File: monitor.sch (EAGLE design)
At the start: 60 parts, among them IC1 LM1117-5, IC2 LM1117-5, J3 DCJ0202, J4 DCJ0202, J5 DCJ0202, Q1 IRLML2502, T1 BC846, X3 PN61729-S, X4 PN87520-S

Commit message: SPI to PGA
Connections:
- new net OE: U$1G$2.PE6, U$4G$9.OE
- net /CS: now also U$4G$3.IOVCC; no longer U$4G$1.IOVCC
- net CLK: now also U$4G$7.IOVCC; no longer U$4G$2.IOVCC
- net DIN: now also U$4G$5.IOVCC; no longer U$4G$4.IOVCC
- net DOUT: now also U$4G$1.IOVCC; no longer U$4G$3.IOVCC
- net I2C3_SCL: now also U$4G$8.IOVL; no longer U$4G$6.IOVL
- net I2C3_SDA: now also U$4G$6.IOVL; no longer U$4G$5.IOVL
- net SCL: now also U$4G$8.IOVCC; no longer U$4G$6.IOVCC
- net SDA: now also U$4G$6.IOVCC; no longer U$4G$5.IOVCC
- net SPI2_MISO: now also U$4G$1.IOVL; no longer U$4G$3.IOVL
- net SPI2_MOSI: now also U$4G$5.IOVL; no longer U$4G$4.IOVL
- net SPI2_NSS: now also U$4G$3.IOVL; no longer U$4G$1.IOVL
- net SPI2_SCK: now also U$4G$7.IOVL; no longer U$4G$2.IOVL
- net VDD: no longer U$1G$2.VDD
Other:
- moved on the sheet: U$4G$1, U$4G$2, U$4G$3, U$4G$4, U$4G$5, U$4G$6
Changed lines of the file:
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@@
 <part name="VDD1" library="supply1" deviceset="VDD" device=""/>
 <part name="VDD2" library="supply1" deviceset="VDD" device=""/>
-<part name="VDD3" library="supply1" deviceset="VDD" device=""/>
 <part name="P+1" library="supply1" deviceset="+5V" device=""/>
 <part name="VDD4" library="supply1" deviceset="VDD" device=""/>
@@
 <instance part="U$3" gate="G$1" x="139.7" y="60.96"/>
 <instance part="GND16" gate="1" x="144.78" y="38.1"/>
-<instance part="U$4" gate="G$1" x="73.66" y="109.22"/>
-<instance part="U$4" gate="G$2" x="73.66" y="99.06"/>
-<instance part="U$4" gate="G$3" x="73.66" y="88.9"/>
-<instance part="U$4" gate="G$4" x="73.66" y="78.74"/>
-<instance part="U$4" gate="G$5" x="73.66" y="68.58"/>
-<instance part="U$4" gate="G$6" x="73.66" y="58.42"/>
+<instance part="U$4" gate="G$3" x="73.66" y="109.22"/>
+<instance part="U$4" gate="G$7" x="73.66" y="99.06"/>
+<instance part="U$4" gate="G$1" x="73.66" y="88.9"/>
+<instance part="U$4" gate="G$5" x="73.66" y="78.74"/>
+<instance part="U$4" gate="G$6" x="73.66" y="68.58"/>
+<instance part="U$4" gate="G$8" x="73.66" y="58.42"/>
 <instance part="U$4" gate="G$9" x="30.48" y="68.58"/>
 <instance part="GND15" gate="1" x="231.14" y="66.04"/>
@@
 <instance part="F1" gate="G$1" x="78.74" y="144.78"/>
 <instance part="D3" gate="1" x="91.44" y="137.16" rot="R90"/>
+<instance part="U$4" gate="G$2" x="73.66" y="48.26"/>
+<instance part="U$4" gate="G$4" x="73.66" y="38.1"/>
 </instances>
 <busses>
@@
 <wire x1="58.42" y1="109.22" x2="48.26" y2="109.22" width="0.1524" layer="91"/>
 <label x="48.26" y="109.22" size="1.778" layer="95"/>
-<pinref part="U$4" gate="G$1" pin="IOVL"/>
+<pinref part="U$4" gate="G$3" pin="IOVL"/>
 </segment>
 </net>
@@
 <wire x1="58.42" y1="88.9" x2="48.26" y2="88.9" width="0.1524" layer="91"/>
 <label x="48.26" y="88.9" size="1.778" layer="95"/>
-<pinref part="U$4" gate="G$3" pin="IOVL"/>
+<pinref part="U$4" gate="G$1" pin="IOVL"/>
 </segment>
 </net>
@@
 <wire x1="58.42" y1="99.06" x2="48.26" y2="99.06" width="0.1524" layer="91"/>
 <label x="48.26" y="99.06" size="1.778" layer="95"/>
-<pinref part="U$4" gate="G$2" pin="IOVL"/>
+<pinref part="U$4" gate="G$7" pin="IOVL"/>
 </segment>
 </net>
@@
 <wire x1="58.42" y1="78.74" x2="48.26" y2="78.74" width="0.1524" layer="91"/>
 <label x="48.26" y="78.74" size="1.778" layer="95"/>
-<pinref part="U$4" gate="G$4" pin="IOVL"/>
+<pinref part="U$4" gate="G$5" pin="IOVL"/>
 </segment>
 </net>
@@
 <wire x1="91.44" y1="109.22" x2="99.06" y2="109.22" width="0.1524" layer="91"/>
 <label x="93.98" y="109.22" size="1.778" layer="95"/>
-<pinref part="U$4" gate="G$1" pin="IOVCC"/>
+<pinref part="U$4" gate="G$3" pin="IOVCC"/>
 </segment>
 <segment>
@@
 <wire x1="91.44" y1="99.06" x2="99.06" y2="99.06" width="0.1524" layer="91"/>
 <label x="93.98" y="99.06" size="1.778" layer="95"/>
-<pinref part="U$4" gate="G$2" pin="IOVCC"/>
+<pinref part="U$4" gate="G$7" pin="IOVCC"/>
 </segment>
 <segment>
@@
 <wire x1="91.44" y1="88.9" x2="99.06" y2="88.9" width="0.1524" layer="91"/>
 <label x="93.98" y="88.9" size="1.778" layer="95"/>
-<pinref part="U$4" gate="G$3" pin="IOVCC"/>
+<pinref part="U$4" gate="G$1" pin="IOVCC"/>
 </segment>
 <segment>
@@
 <wire x1="91.44" y1="78.74" x2="99.06" y2="78.74" width="0.1524" layer="91"/>
 <label x="93.98" y="78.74" size="1.778" layer="95"/>
-<pinref part="U$4" gate="G$4" pin="IOVCC"/>
+<pinref part="U$4" gate="G$5" pin="IOVCC"/>
 </segment>
 <segment>
@@
 <net name="I2C3_SCL" class="0">
 <segment>
-<pinref part="U$4" gate="G$6" pin="IOVL"/>
+<pinref part="U$4" gate="G$8" pin="IOVL"/>
 <wire x1="48.26" y1="58.42" x2="58.42" y2="58.42" width="0.1524" layer="91"/>
 <label x="48.26" y="58.42" size="1.778" layer="95"/>
@@
 </segment>
 <segment>
-<pinref part="U$4" gate="G$5" pin="IOVCC"/>
+<pinref part="U$4" gate="G$6" pin="IOVCC"/>
 <wire x1="91.44" y1="68.58" x2="99.06" y2="68.58" width="0.1524" layer="91"/>
 <label x="93.98" y="68.58" size="1.778" layer="95"/>
@@
 </segment>
 <segment>
-<pinref part="U$4" gate="G$6" pin="IOVCC"/>
+<pinref part="U$4" gate="G$8" pin="IOVCC"/>
 <wire x1="91.44" y1="58.42" x2="99.06" y2="58.42" width="0.1524" layer="91"/>
 <label x="93.98" y="58.42" size="1.778" layer="95"/>
@@
 <net name="I2C3_SDA" class="0">
 <segment>
-<pinref part="U$4" gate="G$5" pin="IOVL"/>
+<pinref part="U$4" gate="G$6" pin="IOVL"/>
 <wire x1="58.42" y1="68.58" x2="48.26" y2="68.58" width="0.1524" layer="91"/>
 <label x="48.26" y="68.58" size="1.778" layer="95"/>
@@
 <pinref part="JP1" gate="B" pin="1"/>
 <wire x1="106.68" y1="147.32" x2="139.7" y2="147.32" width="0.1524" layer="91"/>
+</segment>
+</net>
+<net name="OE" class="0">
+<segment>
+<pinref part="U$4" gate="G$9" pin="OE"/>
+<wire x1="17.78" y1="68.58" x2="10.16" y2="68.58" width="0.1524" layer="91"/>
+<label x="10.16" y="68.58" size="1.778" layer="95"/>
 </segment>
 </net>
@@
 <instance part="VDD1" gate="G$1" x="91.44" y="109.22" rot="R270"/>
 <instance part="VDD2" gate="G$1" x="22.86" y="109.22" rot="R90"/>
-<instance part="VDD3" gate="G$1" x="236.22" y="86.36" rot="R270"/>
 <instance part="P+4" gate="1" x="167.64" y="109.22" smashed="yes" rot="R90">
 <attribute name="VALUE" x="167.64" y="109.22" size="1.778" layer="96" rot="R180"/>
@@
 <pinref part="VDD2" gate="G$1" pin="VDD"/>
 </segment>
-<segment>
-<pinref part="U$1" gate="G$2" pin="VDD"/>
-<pinref part="VDD3" gate="G$1" pin="VDD"/>
-</segment>
 </net>
 <net name="+5V" class="0">
@@
 </segment>
 </net>
+<net name="OE" class="0">
+<segment>
+<pinref part="U$1" gate="G$2" pin="PE6"/>
+<wire x1="170.18" y1="99.06" x2="162.56" y2="99.06" width="0.1524" layer="91"/>
+<label x="162.56" y="99.06" size="1.778" layer="95"/>
+</segment>
+</net>

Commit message: All chips connected
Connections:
- net OUT: no longer U$2.V6
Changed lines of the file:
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@@
 <instance part="F1" gate="G$1" x="78.74" y="144.78"/>
 <instance part="D3" gate="1" x="91.44" y="137.16" rot="R90"/>
-<instance part="U$4" gate="G$2" x="73.66" y="48.26"/>
-<instance part="U$4" gate="G$4" x="73.66" y="38.1"/>
 </instances>
 <busses>
@@
 <junction x="154.94" y="142.24"/>
 </segment>
-<segment>
-<pinref part="U$2" gate="G$1" pin="V6"/>
-<wire x1="187.96" y1="68.58" x2="177.8" y2="68.58" width="0.1524" layer="91"/>
-<label x="177.8" y="68.58" size="1.4224" layer="95"/>
-</segment>
-</net>
+</net>

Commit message: All connected (not routed), updated STM32F4Discovery layout
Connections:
- net B_DOWN: now also U$1G$2.PB7
- net B_ESC: now also U$1G$2.PB5
- net B_LEFT: now also U$1G$2.PE5
- net B_OK: now also U$1G$2.PE3
- net B_RIGHT: now also U$1G$2.PB8
- net B_UP: now also U$1G$2.PE4
- net LCD_CS1: now also U$1G$1.PA2; no longer U$1G$1.PA2/ETH_MDIO
- net LCD_CS2: now also U$1G$1.PC4; no longer U$1G$1.PC4/ETH_MII_RX_D0
- net SPI2_NSS: now also U$1G$1.PB12; no longer U$1G$1.PB12/ETH_MII_TXD0
- net SPI2_SCK: now also U$1G$1.PB13; no longer U$1G$1.PB13/ETH_MII_TXD1
- net VDD: now also U$1G$1.VDD1, U$1G$1.VDD2; no longer U$1G$1.VDO1, U$1G$1.VDO2
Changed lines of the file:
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@@
 <net name="SPI2_NSS" class="0">
 <segment>
-<pinref part="U$1" gate="G$1" pin="PB12/ETH_MII_TXD0"/>
+<pinref part="U$1" gate="G$1" pin="PB12"/>
 <wire x1="88.9" y1="68.58" x2="96.52" y2="68.58" width="0.1524" layer="91"/>
 <label x="96.52" y="68.58" size="1.778" layer="95"/>
@@
 <net name="SPI2_SCK" class="0">
 <segment>
-<pinref part="U$1" gate="G$1" pin="PB13/ETH_MII_TXD1"/>
+<pinref part="U$1" gate="G$1" pin="PB13"/>
 <wire x1="25.4" y1="66.04" x2="17.78" y2="66.04" width="0.1524" layer="91"/>
 <label x="17.78" y="66.04" size="1.778" layer="95"/>
@@
 <net name="VDD" class="0">
 <segment>
-<pinref part="U$1" gate="G$1" pin="VDO2"/>
+<pinref part="U$1" gate="G$1" pin="VDD2"/>
 <pinref part="VDD1" gate="G$1" pin="VDD"/>
 </segment>
 <segment>
-<pinref part="U$1" gate="G$1" pin="VDO1"/>
+<pinref part="U$1" gate="G$1" pin="VDD1"/>
 <pinref part="VDD2" gate="G$1" pin="VDD"/>
 </segment>
@@
 <net name="LCD_CS1" class="0">
 <segment>
-<pinref part="U$1" gate="G$1" pin="PA2/ETH_MDIO"/>
+<pinref part="U$1" gate="G$1" pin="PA2"/>
 <wire x1="88.9" y1="96.52" x2="96.52" y2="96.52" width="0.1524" layer="91"/>
 <label x="96.52" y="96.52" size="1.778" layer="95"/>
@@
 <net name="LCD_CS2" class="0">
 <segment>
-<pinref part="U$1" gate="G$1" pin="PC4/ETH_MII_RX_D0"/>
+<pinref part="U$1" gate="G$1" pin="PC4"/>
 <wire x1="88.9" y1="88.9" x2="96.52" y2="88.9" width="0.1524" layer="91"/>
 <label x="96.52" y="88.9" size="1.778" layer="95"/>
@@
 </segment>
 </net>
+<net name="B_UP" class="0">
+<segment>
+<pinref part="U$1" gate="G$2" pin="PE4"/>
+<wire x1="170.18" y1="96.52" x2="162.56" y2="96.52" width="0.1524" layer="91"/>
+<label x="162.56" y="96.52" size="1.778" layer="95"/>
+</segment>
+</net>
+<net name="B_LEFT" class="0">
+<segment>
+<pinref part="U$1" gate="G$2" pin="PE5"/>
+<wire x1="233.68" y1="96.52" x2="241.3" y2="96.52" width="0.1524" layer="91"/>
+<label x="241.3" y="96.52" size="1.778" layer="95"/>
+</segment>
+</net>
+<net name="B_OK" class="0">
+<segment>
+<pinref part="U$1" gate="G$2" pin="PE3"/>
+<wire x1="233.68" y1="93.98" x2="241.3" y2="93.98" width="0.1524" layer="91"/>
+<label x="241.3" y="93.98" size="1.778" layer="95"/>
+</segment>
+</net>
+<net name="B_DOWN" class="0">
+<segment>
+<pinref part="U$1" gate="G$2" pin="PB7"/>
+<wire x1="233.68" y1="83.82" x2="241.3" y2="83.82" width="0.1524" layer="91"/>
+<label x="241.3" y="83.82" size="1.778" layer="95"/>
+</segment>
+</net>
+<net name="B_ESC" class="0">
+<segment>
+<pinref part="U$1" gate="G$2" pin="PB5"/>
+<wire x1="233.68" y1="81.28" x2="241.3" y2="81.28" width="0.1524" layer="91"/>
+<label x="241.3" y="81.28" size="1.778" layer="95"/>
+</segment>
+</net>
+<net name="B_RIGHT" class="0">
+<segment>
+<pinref part="U$1" gate="G$2" pin="PB8"/>
+<wire x1="170.18" y1="88.9" x2="162.56" y2="88.9" width="0.1524" layer="91"/>
+<label x="162.56" y="88.9" size="1.778" layer="95"/>
+</segment>
+</net>

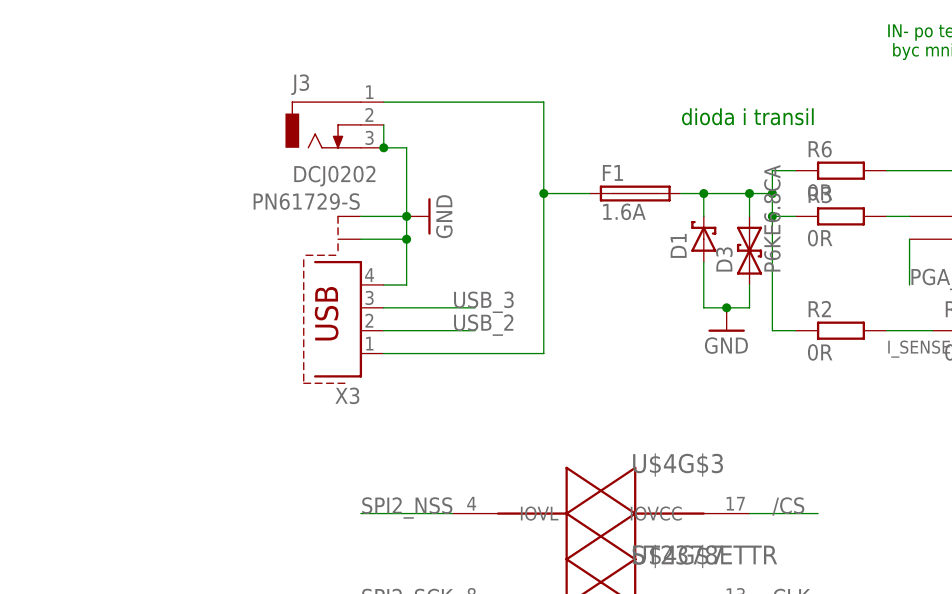
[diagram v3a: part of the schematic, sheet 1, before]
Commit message: All routed, drill diameter increased
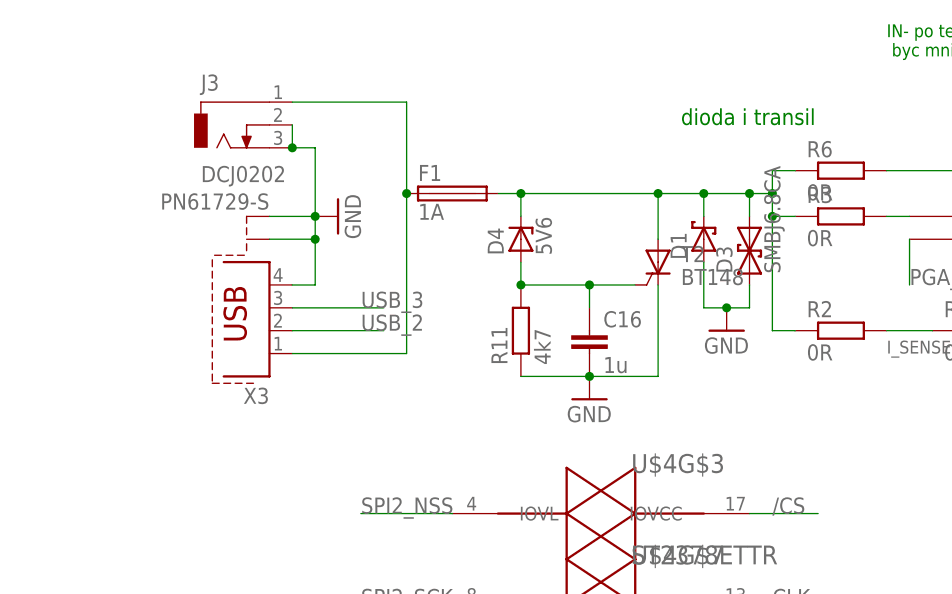
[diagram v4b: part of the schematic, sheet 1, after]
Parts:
- added C16: 1u, rcl:C-EUC0805
- added D4: 5V6, diode:ZENER-DIODESOD80C
- added R11: 4k7, rcl:R-EU_R0805
- added T2: BT148, mgr_components:BT148
- D3: value P6KE6.8CA -> SMBJ6.8CA; device diode:P6KEXXC -> mgr_components:SMBJ
- F1: value 1.6A -> 1A
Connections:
- new net N$23: C16.1, D4.A, R11.2, T2.G
- net GND: now also C16.2, R11.1, T2.C
- net N$13: now also D4.C, T2.A
- net N$17: now also UP.P1
- net N$18: now also RIGHT.P1
- net N$19: now also DOWN.P1
- net N$20: now also ESC.P1
- net N$21: now also OK.P1
- net N$7: now also LEFT.P1
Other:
- moved on the sheet: F1, J3, X3

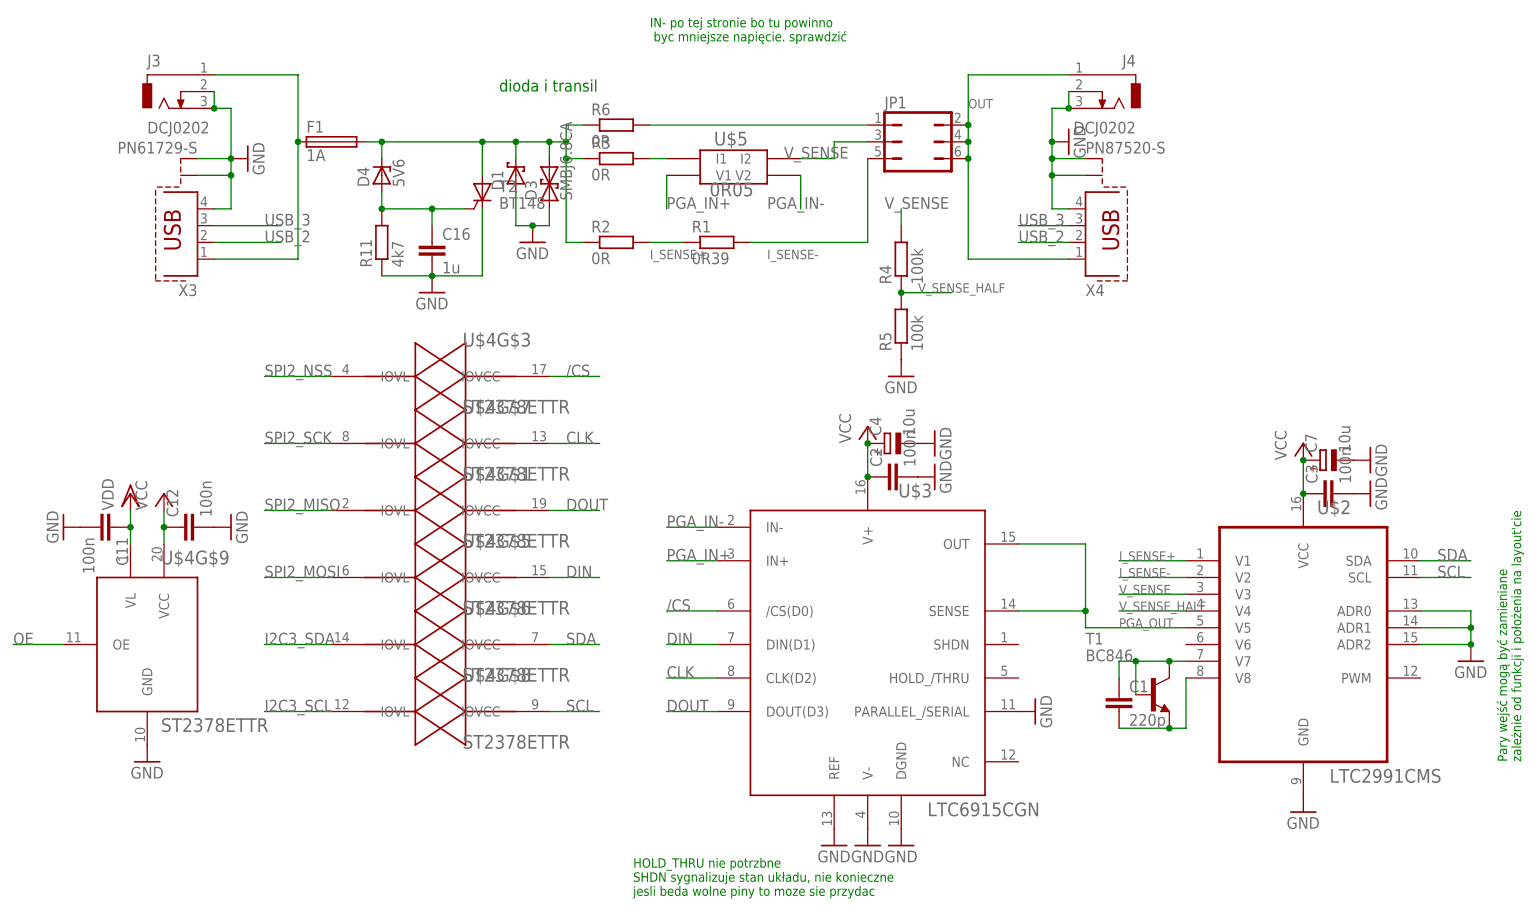
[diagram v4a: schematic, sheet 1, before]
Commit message: Added inductors on analog supply. Rerouted some signals.
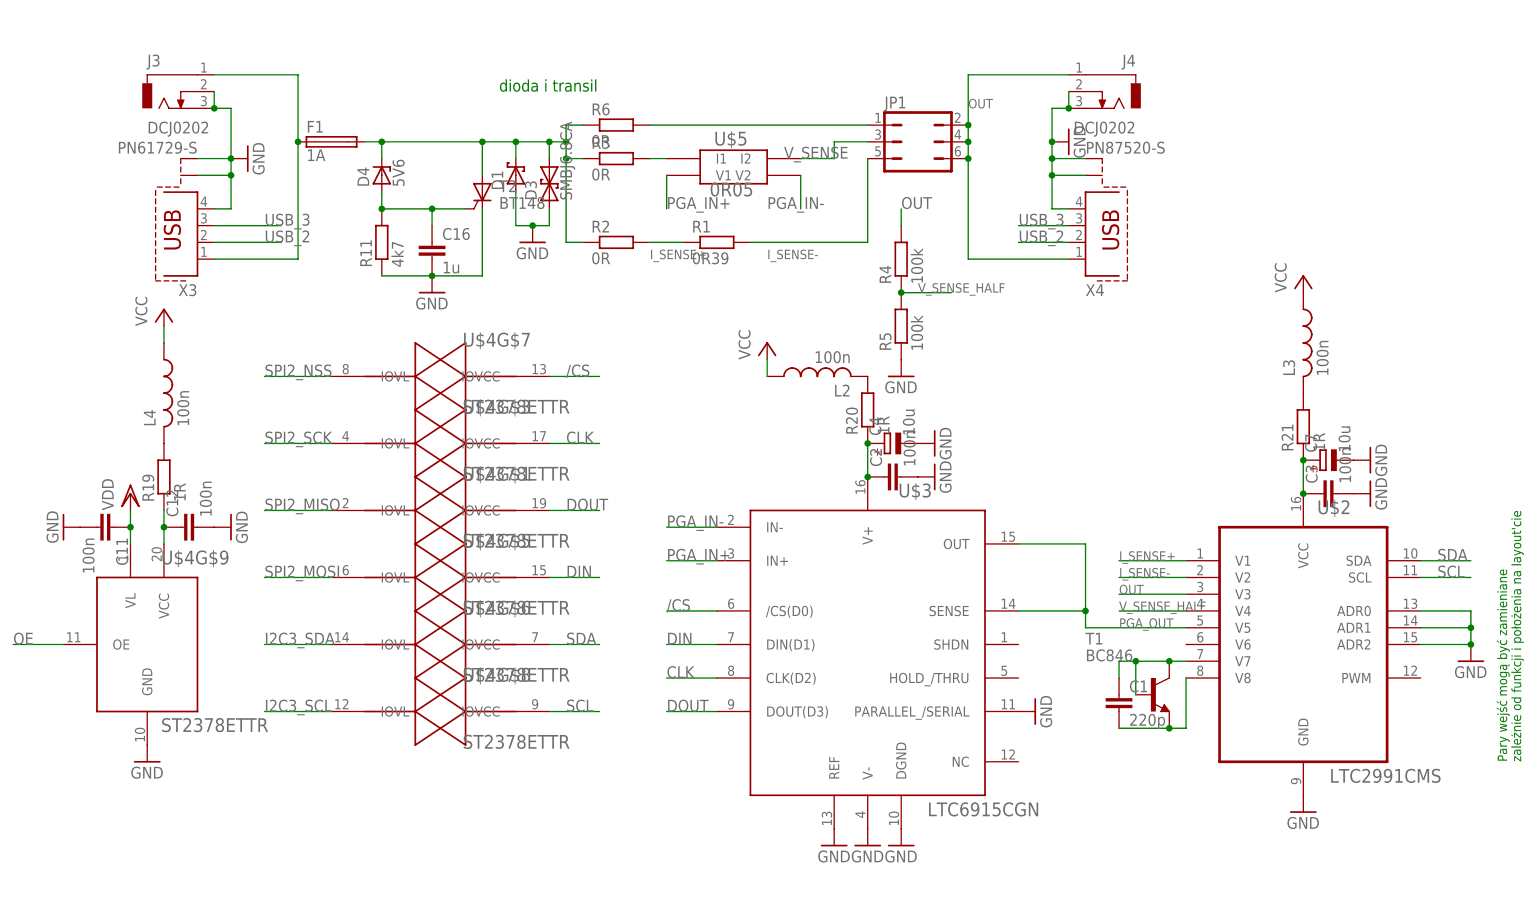
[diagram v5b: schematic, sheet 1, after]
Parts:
- added L1, L2, L3, L4: 100n, rcl:L-US
- added R18, R19, R20, R21: 1R, rcl:R-EU_R0603
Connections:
- new net N$24: L1.1, R18.2
- new net N$25: JP2.2, R18.1
- new net N$27: C12.1, R19.1, U$4G$9.VCC
- new net N$30: L4.2, R19.2
- new net N$31: C2.1, C4.+, R20.1, U$3.V+
- new net N$32: C3.1, C7.+, R21.1, U$2.VCC
- new net N$33: L2.2, R20.2
- new net N$35: L3.2, R21.2
- net /CS: now also U$4G$7.IOVCC; no longer U$4G$3.IOVCC
- net CLK: now also U$4G$3.IOVCC; no longer U$4G$7.IOVCC
- net N$17: no longer UP.P1
- net OUT: now also R4.2, U$2.V3
- net SPI2_NSS: now also U$4G$7.IOVL; no longer U$4G$3.IOVL
- net SPI2_SCK: now also U$4G$3.IOVL; no longer U$4G$7.IOVL
- net VCC: now also L1.2, L2.1, L3.1, L4.1; no longer C12.1, C2.1, C3.1, C4.+, C7.+, JP2.2, U$2.VCC, U$3.V+, U$4G$9.VCC
- net V_SENSE: no longer R4.2, U$2.V3
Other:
- note removed: "HOLD_THRU nie potrzbne SHDN sygnalizuje stan układu, nie konieczne jesli beda wolne piny to moze sie przydac"
- note removed: "IN- po tej stronie bo tu powinno byc mniejsze napięcie. sprawdzić"
- moved on the sheet: U$4G$3, U$4G$7

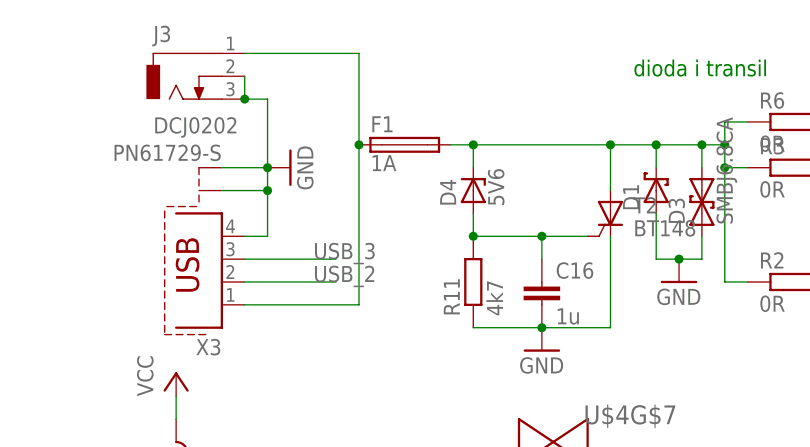
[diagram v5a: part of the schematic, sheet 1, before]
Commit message: Extra vias
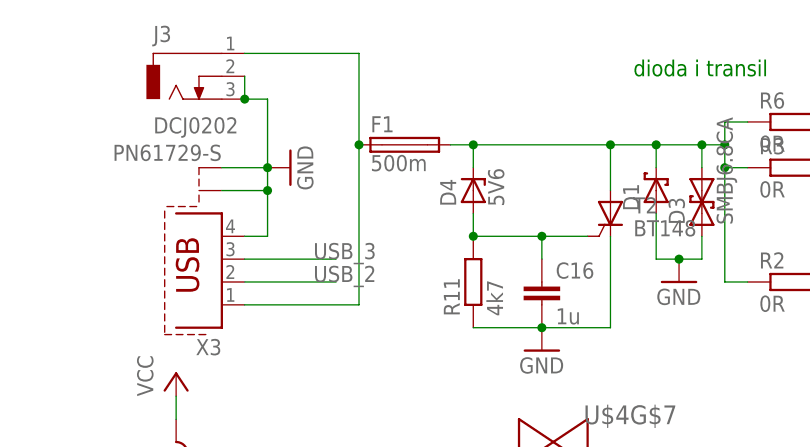
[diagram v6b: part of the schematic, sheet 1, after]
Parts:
- F1: value 1A -> 500m
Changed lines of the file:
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@@
 <part name="R10" library="rcl" deviceset="R-EU_" device="R0805" value="100"/>
 <part name="P+7" library="supply1" deviceset="+5V" device=""/>
-<part name="F1" library="fuse" deviceset="FUSE" device="1206" value="1A"/>
+<part name="F1" library="fuse" deviceset="FUSE" device="1206" value="500m"/>
 <part name="D3" library="mgr_components" deviceset="SMBJ" device="" value="SMBJ6.8CA"/>
 <part name="R12" library="rcl" deviceset="R-EU_" device="R0805" value="330"/>
